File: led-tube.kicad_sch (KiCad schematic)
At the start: 71 parts, among them SW3 TS-1185EC-C-D-B, U1 ESP32-WROOM-32E, U4 BL1117-33CX, U6 SN74AHCT32QPWRQ1

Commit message: delete copied pcb
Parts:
- removed U1: ESP32-WROOM-32E, footprint:WIFI-SMD_ESP32-WROOM-32E, symbol GLOWINGKITTYPARTS:ESP32-WROOM-32E
- added U1: QuinLED-ESP32, quinled:QuinLED-ESP32, symbol quinled:QuinLED-ESP32
- added U2: U262-161N-4BVC11, footprint:USB-3.1-SMD_U262-161N-4BVC11, symbol GLOWINGKITTYPARTS:U262-161N-4BVC11
- gave numbers to parts that had none: 1
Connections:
- net +3V3: no longer C1.1
- net +5V: now also C1.1, U1.26 (5v0)
- net GND: now also U1.1 (GND), U1.2 (GND*), U1.25 (GND), U1.28 (GND), U2.A1B12 (GND), U2.B1A12 (GND), U2.SHELL
- net IO16/LED1: now also U1.24 (IO16)
- net IO33/MAINBUTTON: now also U1.5 (IO33)
- net VBUS: now also U2.A4B9 (VBUS), U2.B4A9 (VBUS)
- new net USB-C CC1: U2.A5 (CC1)
- new net USB-C CC2: U2.B5 (CC2)
- new net USB-C DATA +: U2.A6 (DP1), U2.B6 (DP2)
- new net USB-C DATA -: U2.A7 (DN1), U2.B7 (DN2)
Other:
- note added: "USB-C Port"
- moved on the sheet: C2, R1, SW3, U6

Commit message: delete old drawings, place Power Bank IC
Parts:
- added BT1, BT2, BT3, BT4: BH-18650-B1BA002, easyeda2kicad:BATTERY-SMD_18650-1S-L77.1-W20.7-1, symbol easyeda2kicad:BH-18650-B1BA002
- added C12, C42, C44: 100nf, Capacitor_SMD:C_0603_1608Metric_Pad1.08x0.95mm_HandSolder, symbol Device:C
- added C13, C38, C39, C40, C43, C45, C46, C47, C48: 22uf, Capacitor_SMD:C_0805_2012Metric_Pad1.18x1.45mm_HandSolder, symbol Device:C
- added C41, C51, C52: 10uf, Capacitor_SMD:C_0603_1608Metric_Pad1.08x0.95mm_HandSolder, symbol Device:C
- added C49, C50: 2.2uf, Capacitor_SMD:C_0603_1608Metric_Pad1.08x0.95mm_HandSolder, symbol Device:C
- added C53, C54, C55, C56, C57, C58, C59, C60, C61, C62: 0.1uF, Capacitor_SMD:C_0603_1608Metric_Pad1.08x0.95mm_HandSolder, symbol Device:C
- added L1: MDA1050-2R2M, easyeda2kicad:IND-SMD_L11.0-W10.0, symbol easyeda2kicad:MDA1050-2R2M
- added LED31, LED32, LED33, LED34, LED35, LED36, LED37, LED38, LED39, LED40: XL-5050RGBC-WS2812B, LED_SMD:LED_WS2812B_PLCC4_5.0x5.0mm_P3.2mm, symbol GLOWINGKITTYPARTS:XL-5050RGBC-WS2812B
- added Q1, Q2: RU20P7C_C605444, easyeda2kicad:SOT-23-3_L2.9-W1.6-P1.90-LS2.8-BR, symbol easyeda2kicad:RU20P7C_C605444
- added R10, R13: 10k, Resistor_SMD:R_0603_1608Metric_Pad0.98x0.95mm_HandSolder, symbol Device:R
- added R11, R12: 5.1k, Resistor_SMD:R_0603_1608Metric_Pad0.98x0.95mm_HandSolder, symbol Device:R
- added R2: 113k, Resistor_SMD:R_0603_1608Metric_Pad0.98x0.95mm_HandSolder, symbol Device:R
- added R3: 0.01, Resistor_SMD:R_0603_1608Metric_Pad0.98x0.95mm_HandSolder, symbol Device:R
- added R4, R5, R6, R7, R9: 100, Resistor_SMD:R_0603_1608Metric_Pad0.98x0.95mm_HandSolder, symbol Device:R
- added R8: 82k, Resistor_SMD:R_0603_1608Metric_Pad0.98x0.95mm_HandSolder, symbol Device:R
- added RT1: TCTR0805F100KF4000T, easyeda2kicad:R0805, symbol easyeda2kicad:TCTR0805F100KF4000T
- added SW1: TS-1185EC-C-D-B, footprint:SW-SMD_4P-L3.7-W3.0-P1.50-LS4.7, symbol GLOWINGKITTYPARTS:TS-1185EC-C-D-B
- added U10, U5, U7, U8, U9: 19-217_R6C-AL1M2VY_3T, footprint:LED0603-R-RD, symbol GLOWINGKITTYPARTS:19-217_R6C-AL1M2VY_3T
- added U3: IP5328P, easyeda2kicad:QFN-40_L6.0-W6.0-P0.50-BL-EP, symbol easyeda2kicad:IP5328P
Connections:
- net +5V: now also C52.1, C53.2, C54.2, C55.2, C56.2, C57.2, C58.2, C59.2, C60.2, C61.2, C62.2, LED31.1 (VDD), LED32.1 (VDD), LED33.1 (VDD), LED34.1 (VDD), LED35.1 (VDD), LED36.1 (VDD), LED37.1 (VDD), LED38.1 (VDD), LED39.1 (VDD), LED40.1 (VDD), Q2.3 (D), U3.37 (VOUT1)
- net GND: now also SW3.2, BT1.1, BT2.1, BT3.1, BT4.1, C12.1, C13.2, C38.2, C39.2, C40.2, C41.2, C42.2, C43.2, C45.2, C46.2, C47.2, C48.2, C49.2, C50.1, C51.2, C53.1, C54.1, C55.1, C56.1, C57.1, C58.1, C59.1, C60.1, C61.1, C62.1, LED31.4 (GND), LED32.4 (GND), LED33.4 (GND), LED34.4 (GND), LED35.4 (GND), LED36.4 (GND), LED37.4 (GND), LED38.4 (GND), LED39.4 (GND), LED40.4 (GND), R11.2, R12.1, R2.2, R7.1, R8.1, RT1.2, SW1.2, U3.29 (AGND), U5.2 (C); no longer SW3.1
- net IO33/MAINBUTTON: now also SW3.1; no longer SW3.2
- net USB-C CC1: now also U3.2 (CC1)
- net USB-C CC2: now also U3.3 (CC2)
- net USB-C DATA +: now also U3.5 (DPC)
- net USB-C DATA -: now also U3.4 (DMC)
- net VBUS: now also C51.1, Q1.3 (D), U3.32 (VBUS)
- net at LED30.2 (DO): now also LED31.3 (DI)
- new net: R6.2, U7.1 (A), U8.2 (C)
- new net: R7.2, U10.2 (C), U7.2 (C), U8.1 (A), U9.1 (A)
- new net: LED35.2 (DO), LED36.3 (DI)
- new net: LED34.2 (DO), LED35.3 (DI)
- new net: LED31.2 (DO), LED32.3 (DI)
- new net: LED33.2 (DO), LED34.3 (DI)
- new net: LED32.2 (DO), LED33.3 (DI)
- new net: R13.1, U3.34 (VOUT2)
- new net: LED39.2 (DO), LED40.3 (DI)
- new net: LED38.2 (DO), LED39.3 (DI)
- new net: LED37.2 (DO), LED38.3 (DI)
- new net: R8.2, RT1.1, U3.10 (NTC)
- new net: R5.1, U3.11 (L1)
- new net: R6.1, U3.12 (L2)
- new net: C44.1, L1.1, U3.14 (LX), U3.15 (LX), U3.16 (LX), U3.17 (LX), U3.18 (LX)
- new net: C44.2, U3.19 (BST)
- new net: R4.1, U3.20 (LIGHT)
- new net: R2.1, U3.21 (RSET)
- new net: R5.2, U10.1 (A), U9.2 (C)
- new net: LED36.2 (DO), LED37.3 (DI)
- new net: R9.2, SW1.1
- new net: R4.2, U5.1 (A)
- new net DMA1: R11.1, U3.38 (DMA1)
- new net DPA1: R12.2, U3.39 (DPA1)
- new net KEY: R9.1, U3.26 (KEY)
- new net VBAT: BT1.2, BT2.2, BT3.2, BT4.2, C45.1, C46.1, C47.1, C48.1, C50.2, L1.2, U3.28 (BAT)
- new net VBUSG: Q1.1 (G), R10.2, U3.33 (VBUSG)
- new net VMID: C42.1, C43.1, Q1.2 (S), Q2.2 (S), R10.1, R3.2, U3.25 (VSN)
- new net VOUT1G: Q2.1 (G), U3.36 (VOUT1G)
- new net VREG: C49.1, R13.2, U3.27 (VREG)
- new net VSYS: C12.2, C13.1, C38.1, C39.1, C40.1, C41.1, R3.1, U3.22 (VSYS), U3.23 (VSYS), U3.24 (VSP), U3.8 (VSYS), U3.9 (VSYS)
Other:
- note added: "Buttons"
- note added: "Not entierly sure, if need to pull DMA1 and DPA1 to 5.1k with resistors, or short, or do nothing to pull full 5v 3.1a. Might not place these resistors at first..."
- note added: "Power Bank IC"
- note added: "Power Output from Power Bank IC to Power the 5v rail. This would be a USB-A output port in the reference design."
- note added: "This is to make sure the datasignal for the LEDs is 5v"
- note removed: "Main button"
- note removed: "This is to make sure the datasignal is 5v"
- moved on the sheet: C14, C15, C16, C2, F1, R1, SW3, U2, U4, U6

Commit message: connect unconnected pieces, add micro usb for charging
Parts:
- removed C15: 10uF, Capacitor_SMD:C_0603_1608Metric_Pad1.08x0.95mm_HandSolder, symbol Device:C
- removed C16: 220uF, Capacitor_SMD:C_Elec_6.3x5.4, symbol Device:C
- removed F1: BSMD1812-300-16V, footprint:F1812, symbol GLOWINGKITTYPARTS:BSMD1812-300-16V
- removed U4: BL1117-33CX, footprint:SOT-223-4_L6.5-W3.5-P2.30-LS7.0-BR, symbol GLOWINGKITTYPARTS:BL1117-33CX
- added C63: CS1E102M-CRI13, easyeda2kicad:CAP-SMD_BD12.5-L13.0-W13.0-FD, symbol easyeda2kicad:CS1E102M-CRI13
- added F2: BSMD1812-350-16V, easyeda2kicad:F1812, symbol easyeda2kicad:BSMD1812-350-16V
- added Q3: RU20P7C_C605444, easyeda2kicad:SOT-23-3_L2.9-W1.6-P1.90-LS2.8-BR, symbol easyeda2kicad:RU20P7C_C605444
- added U11, U12, U13, U14, U15: SMTSO3015CTJ, footprint:SMTSO3030CTJ, symbol GLOWINGKITTYPARTS:SMTSO3015CTJ
- added USB1: MICROXNJ, easyeda2kicad:MICRO-USB-SMD_MICROXNJ, symbol easyeda2kicad:MICROXNJ
- C14: value 10uF -> 10uf
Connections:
- net +5V: now also C63.1, F2.2, U14.1; no longer C14.1, C52.1, Q2.3 (D), U3.37 (VOUT1)
- net GND: now also C52.2, U3.41 (EPAD), C63.2, U11.1, U12.1, U13.1, USB1.4 (ID), USB1.5 (GND), USB1.6 (SH1), USB1.7 (SH2), USB1.8 (SH3), USB1.9 (SH4)
- net VMID: now also Q3.2 (S)
- net at R7.2, U10.2 (C), U7.2 (C)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: now also U3.13 (L3)
- net IO34/SECOND BUTTON: now reaches U1.6 (IO34)
- net VIN: now reaches U3.30 (VIN)
- net VIN: now also C14.1, Q3.3 (D), USB1.1 (VBUS)
- net VING: now reaches U3.31 (VING)
- net VING: now also Q3.1 (G)
- net DMB: now reaches U3.6 (DMB)
- net DMB: now also USB1.3 (D+)
- net DPB: now reaches U3.7 (DPB)
- net DPB: now also USB1.2 (D-)
- net LED DATA NEXT BOARD: now reaches LED40.2 (DO)
- net LED DATA NEXT BOARD: now also U15.1
- new net VOUT1: C52.1, F2.1, Q2.3 (D), U3.37 (VOUT1)
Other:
- note added: "18650 Lithium Battery Cells"
- note added: "Capacitor behind fuse 1000uF"
- note added: "Fuse 3.5A 16v"
- note added: "Not entierly sure, if it is needed to pull DMA1 and DPA1 to 5.1k with resistors, or short them, or do nothing to get full 5v 3.1a. Might not place these resistors at first, and test out."
- note added: "SMD nuts"
- note added: "mircoUSB Port for Powerbank Input"
- note removed: "Bipolar Linear Regulator 5v to 3.3v"
- note removed: "Capacitor behind fuse"
- note removed: "Fuse 3A 16v"
- note removed: "Not entierly sure, if need to pull DMA1 and DPA1 to 5.1k with resistors, or short, or do nothing to pull full 5v 3.1a. Might not place these resistors at first..."
- moved on the sheet: BT1, BT2, BT3, BT4, C1, C2, C52, Q2, R1, U1, U6

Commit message: update README
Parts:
- removed SW1, SW3: TS-1185EC-C-D-B, footprint:SW-SMD_4P-L3.7-W3.0-P1.50-LS4.7, symbol GLOWINGKITTYPARTS:TS-1185EC-C-D-B
- removed U12, U13: SMTSO3015CTJ, footprint:SMTSO3030CTJ, symbol GLOWINGKITTYPARTS:SMTSO3015CTJ
- added SW1, SW2: K2-1112SW-A4SW-04, easyeda2kicad:KEY-TH_K2-1112SW-AXXW-XX, symbol easyeda2kicad:K2-1112SW-A4SW-04
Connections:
- net GND: now also SW1.2, SW2.2
- net IO33/MAINBUTTON: now also SW2.1
- net at R9.2: now also SW1.1
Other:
- moved on the sheet: U11, U14, U15

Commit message: place components, don't place leds but use ledstrips instead
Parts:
- removed BT3, BT4: BH-18650-B1BA002, easyeda2kicad:BATTERY-SMD_18650-1S-L77.1-W20.7-1, symbol easyeda2kicad:BH-18650-B1BA002
- removed C14, C41: 10uf, Capacitor_SMD:C_0603_1608Metric_Pad1.08x0.95mm_HandSolder, symbol Device:C
- removed C21, C22, C23, C24, C25, C26, C27, C28, C29, C30, C31, C32, C33, C34, C35, C36, C37, C53, C54, C55, C56, C57, C58, C59, C60, C61, C62: 0.1uF, Capacitor_SMD:C_0603_1608Metric_Pad1.08x0.95mm_HandSolder, symbol Device:C
- removed C38, C39, C40, C43, C45, C46, C47, C48: 22uf, Capacitor_SMD:C_0805_2012Metric_Pad1.18x1.45mm_HandSolder, symbol Device:C
- removed C42, C44: 100nf, Capacitor_SMD:C_0603_1608Metric_Pad1.08x0.95mm_HandSolder, symbol Device:C
- removed C49, C50: 2.2uf, Capacitor_SMD:C_0603_1608Metric_Pad1.08x0.95mm_HandSolder, symbol Device:C
- removed F2: BSMD1812-350-16V, easyeda2kicad:F1812, symbol easyeda2kicad:BSMD1812-350-16V
- removed LED1, LED10, LED11, LED12, LED13, LED14, LED15, LED16, LED17, LED18, LED19, LED2, LED20, LED21, LED22, LED23, LED24, LED25, LED26, LED27, LED28, LED29, LED3, LED30, LED31, LED32, LED33, LED34, LED35, LED36, LED37, LED38, LED39, LED4, LED40, LED5, LED6, LED7, LED8, LED9: XL-5050RGBC-WS2812B, LED_SMD:LED_WS2812B_PLCC4_5.0x5.0mm_P3.2mm, symbol GLOWINGKITTYPARTS:XL-5050RGBC-WS2812B
- removed Q3: RU20P7C_C605444, easyeda2kicad:SOT-23-3_L2.9-W1.6-P1.90-LS2.8-BR, symbol easyeda2kicad:RU20P7C_C605444
- removed U10, U5: 19-217_R6C-AL1M2VY_3T, footprint:LED0603-R-RD, symbol GLOWINGKITTYPARTS:19-217_R6C-AL1M2VY_3T
- removed U3: IP5328P, easyeda2kicad:QFN-40_L6.0-W6.0-P0.50-BL-EP, symbol easyeda2kicad:IP5328P
- removed USB1: MICROXNJ, easyeda2kicad:MICRO-USB-SMD_MICROXNJ, symbol easyeda2kicad:MICROXNJ
- added C15: 1uF, Capacitor_SMD:C_0603_1608Metric_Pad1.08x0.95mm_HandSolder, symbol Device:C
- added C16: 0.1uF, Capacitor_SMD:C_0603_1608Metric_Pad1.08x0.95mm_HandSolder, symbol Device:C
- added F1: BSMD2920-500-16V, easyeda2kicad:F2920, symbol easyeda2kicad:BSMD2920-500-16V
- added JP1: SolderJumper_2_Bridged, Jumper:SolderJumper-2_P1.3mm_Bridged_RoundedPad1.0x1.5mm, symbol Jumper:SolderJumper_2_Bridged
- added MIC1: MP34DT05TR-A, easyeda2kicad:MIC-SMD_5P-L3.0-W4.0-P0.85-BL, symbol easyeda2kicad:MP34DT05TR-A
- added P1: WJ15EDGRC-3.81-3P, easyeda2kicad:CONN-TH_3P-P3.81_WJ15EDGRC-3.81-3P, symbol easyeda2kicad:WJ15EDGRC-3.81-3P
- added R14, R15: 100, Resistor_SMD:R_0603_1608Metric_Pad0.98x0.95mm_HandSolder, symbol Device:R
- added SW3: K2-1112SW-A4SW-04, easyeda2kicad:KEY-TH_K2-1112SW-AXXW-XX, symbol easyeda2kicad:K2-1112SW-A4SW-04
- added SW4: SS-12M11G5, easyeda2kicad:SW-TH_XKB_SS-12M11XX, symbol easyeda2kicad:SS-12M11G5
- added U10: SMTSO3015CTJ, footprint:SMTSO3030CTJ, symbol GLOWINGKITTYPARTS:SMTSO3015CTJ
- added U3, U4: 19-217_R6C-AL1M2VY_3T, footprint:LED0603-R-RD, symbol GLOWINGKITTYPARTS:19-217_R6C-AL1M2VY_3T
- added U5: IP5328P, easyeda2kicad:QFN-40_L6.0-W6.0-P0.50-BL-EP, symbol easyeda2kicad:IP5328P
- C10, C11, C17, C18, C19, C20, C5, C8: value 0.1uF -> 22uf; footprint Capacitor_SMD:C_0603_1608Metric_Pad1.08x0.95mm_HandSolder -> Capacitor_SMD:C_0805_2012Metric_Pad1.18x1.45mm_HandSolder
- C12: value 100nf -> 22uf; footprint Capacitor_SMD:C_0603_1608Metric_Pad1.08x0.95mm_HandSolder -> Capacitor_SMD:C_0805_2012Metric_Pad1.18x1.45mm_HandSolder
- C13: value 22uf -> 10uf; footprint Capacitor_SMD:C_0805_2012Metric_Pad1.18x1.45mm_HandSolder -> Capacitor_SMD:C_0603_1608Metric_Pad1.08x0.95mm_HandSolder
- C3, C4: value 0.1uF -> 2.2uf
- C6, C7, C9: value 0.1uF -> 100nf
- R13: value 10k -> 100
- R2: value 113k -> 10k
- R4: value 100 -> 82k
- R5: value 100 -> 113k
- R8: value 82k -> 100
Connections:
- net LED DATA NEXT BOARD is gone; now on net LED DATA OUT: U15.1
- net +5V: now also P1.1, R14.2, R15.2, SW4.2; no longer C10.2, C11.2, C17.2, C18.2, C19.2, C20.2, C3.2, C4.2, C5.2, C6.2, C7.2, C8.2, C9.2
- net DMA1: now also U5.38 (DMA1)
- net DMB: now also U5.6 (DMB)
- net DPA1: now also U5.39 (DPA1)
- net DPB: now also U5.7 (DPB)
- net GND: now also C10.2, C11.2, C12.2, C17.2, C18.2, C19.2, C20.2, C4.2, C5.2, C6.2, C8.2, R13.1, R4.1, R5.2, U8.2 (C), C15.1, C16.1, MIC1.2 (LR), MIC1.5 (GND), P1.3, SW3.2, U10.1, U5.29 (AGND), U5.41 (EPAD); no longer C10.1, C11.1, C12.1, C17.1, C18.1, C19.1, C20.1, C4.1, C5.1, C6.1, C8.1, C9.1, R2.2, R7.1, R8.1
- net IO33/MAINBUTTON: now also R14.1
- net IO34/SECOND BUTTON: now also R15.1, SW3.1
- net KEY: now also U5.26 (KEY)
- net LED DATA OUT: now also P1.2
- net USB-C CC1: now also U5.2 (CC1)
- net USB-C CC2: now also U5.3 (CC2)
- net USB-C DATA +: now also U5.5 (DPC)
- net USB-C DATA -: now also U5.4 (DMC)
- net VBAT: now also C17.1, C18.1, C19.1, C20.1, C3.2, U5.28 (BAT)
- net VBUS: now also U5.32 (VBUS)
- net VBUSG: now also U5.33 (VBUSG)
- net VIN: now also U5.30 (VIN)
- net VING: now also U5.31 (VING)
- net VMID: now also C5.1, C6.1, U5.25 (VSN)
- net VOUT1: now also F1.2, U5.37 (VOUT1)
- net VOUT1G: now also U5.36 (VOUT1G)
- net VREG: now also C4.1, R2.2, U5.27 (VREG); no longer R13.2
- net VSYS: now also C10.1, C11.1, C12.1, C7.2, C8.1, U5.22 (VSYS), U5.23 (VSYS), U5.24 (VSP), U5.8 (VSYS), U5.9 (VSYS); no longer C12.2
- net at R6.2, U7.1 (A): now also U3.2 (C); no longer U8.2 (C)
- net at R7.2, U9.1 (A): now also U4.2 (C); no longer U7.2 (C), U8.1 (A)
- net +3.3V: now reaches U1.17 (3v3)
- net +3.3V: now also JP1.1 (A)
- net IO32/MIC DATA: now reaches U1.31 (IO32)
- net IO32/MIC DATA: now also MIC1.4 (DOUT)
- net IO12/MIC CLK: now reaches U1.32 (IO12)
- net IO12/MIC CLK: now also MIC1.3 (CLK)
- net at R8.2: now also U8.1 (A); no longer RT1.1
- net at R5.1: now also U5.21 (RSET)
- net at R6.1: now also U5.11 (L1)
- net at L1.1: now also C9.1, U5.14 (LX), U5.15 (LX), U5.16 (LX), U5.17 (LX), U5.18 (LX)
- net at R2.1: now also U5.34 (VOUT2)
- net at U9.2 (C): now also R13.2, U7.2 (C), U3.1 (A), U4.1 (A), U5.13 (L3); no longer R5.2
- net at R4.2: now also RT1.1, U5.10 (NTC)
- new net: C15.2, C16.2, JP1.2 (B), MIC1.1 (Vdd)
- new net: C9.2, U5.19 (BST)
- new net: R7.1, U5.12 (L2)
- new net: F1.1, SW4.1
- new net: R8.1, U5.20 (LIGHT)
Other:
- note added: "Connection to LEDs"
- note added: "Fuse 5A 16v"
- note added: "On/Off Switch"
- note added: "PDM Microphone"
- note removed: "Fuse 3.5A 16v"
- note removed: "LEDs"
- note removed: "mircoUSB Port for Powerbank Input"
- moved on the sheet: BT1, BT2, C1, C2, C51, C52, C63, Q1, Q2, R1, R10, R11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

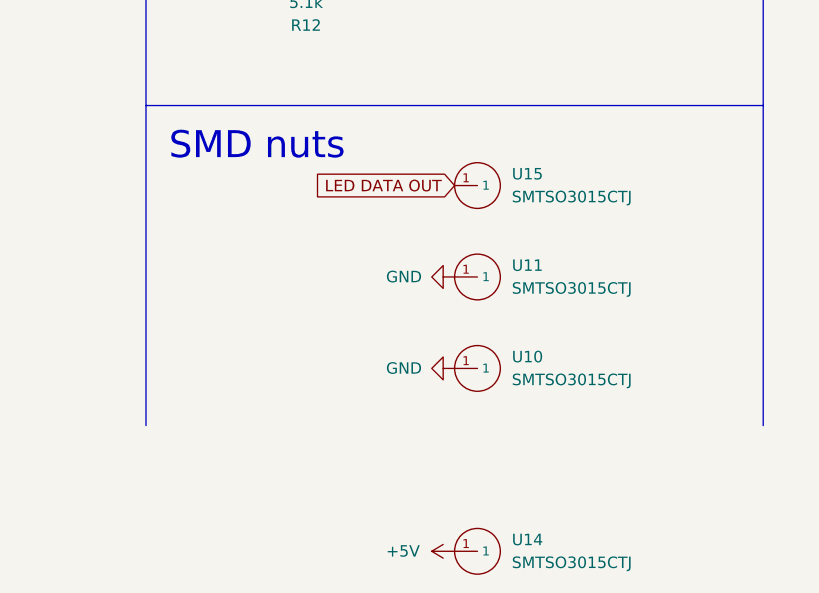
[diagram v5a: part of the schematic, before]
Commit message: add opensource hardware logo
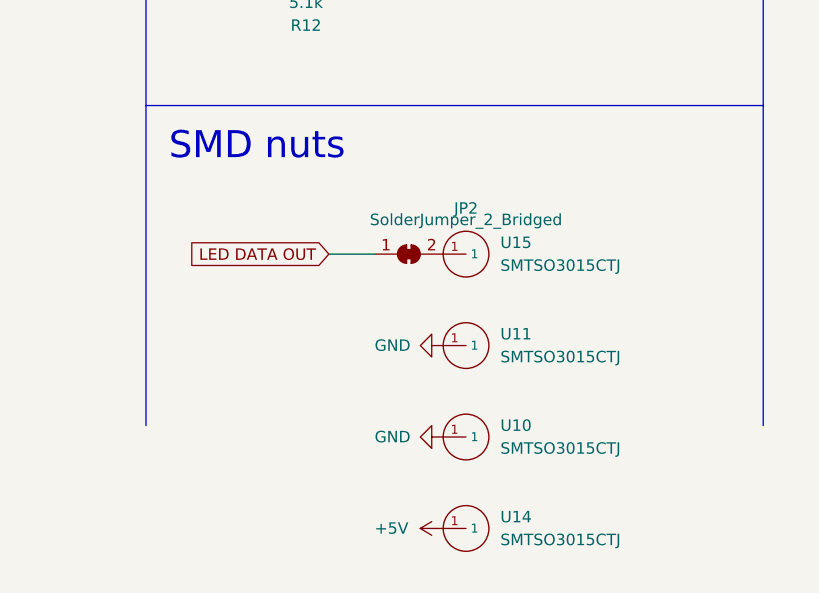
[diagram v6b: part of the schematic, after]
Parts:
- added JP2: SolderJumper_2_Bridged, Jumper:SolderJumper-2_P1.3mm_Bridged_RoundedPad1.0x1.5mm, symbol Jumper:SolderJumper_2_Bridged
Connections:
- net LED DATA OUT: now also JP2.1 (A); no longer U15.1
- new net: JP2.2 (B), U15.1
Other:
- moved on the sheet: U10, U11, U14, U15
